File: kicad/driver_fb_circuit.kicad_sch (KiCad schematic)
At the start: 51 parts, among them Q1 IRFZ44N, Q2 IRFZ44N, Q3 IRFZ44N, Q4 IRFZ44N, Q5 IRFZ44N, Q6 IRFZ44N, U1 IR2104, U2 IR2104, U3 IR2104, U4 INA180A2, U7 INA180A2, U8 INA180A2

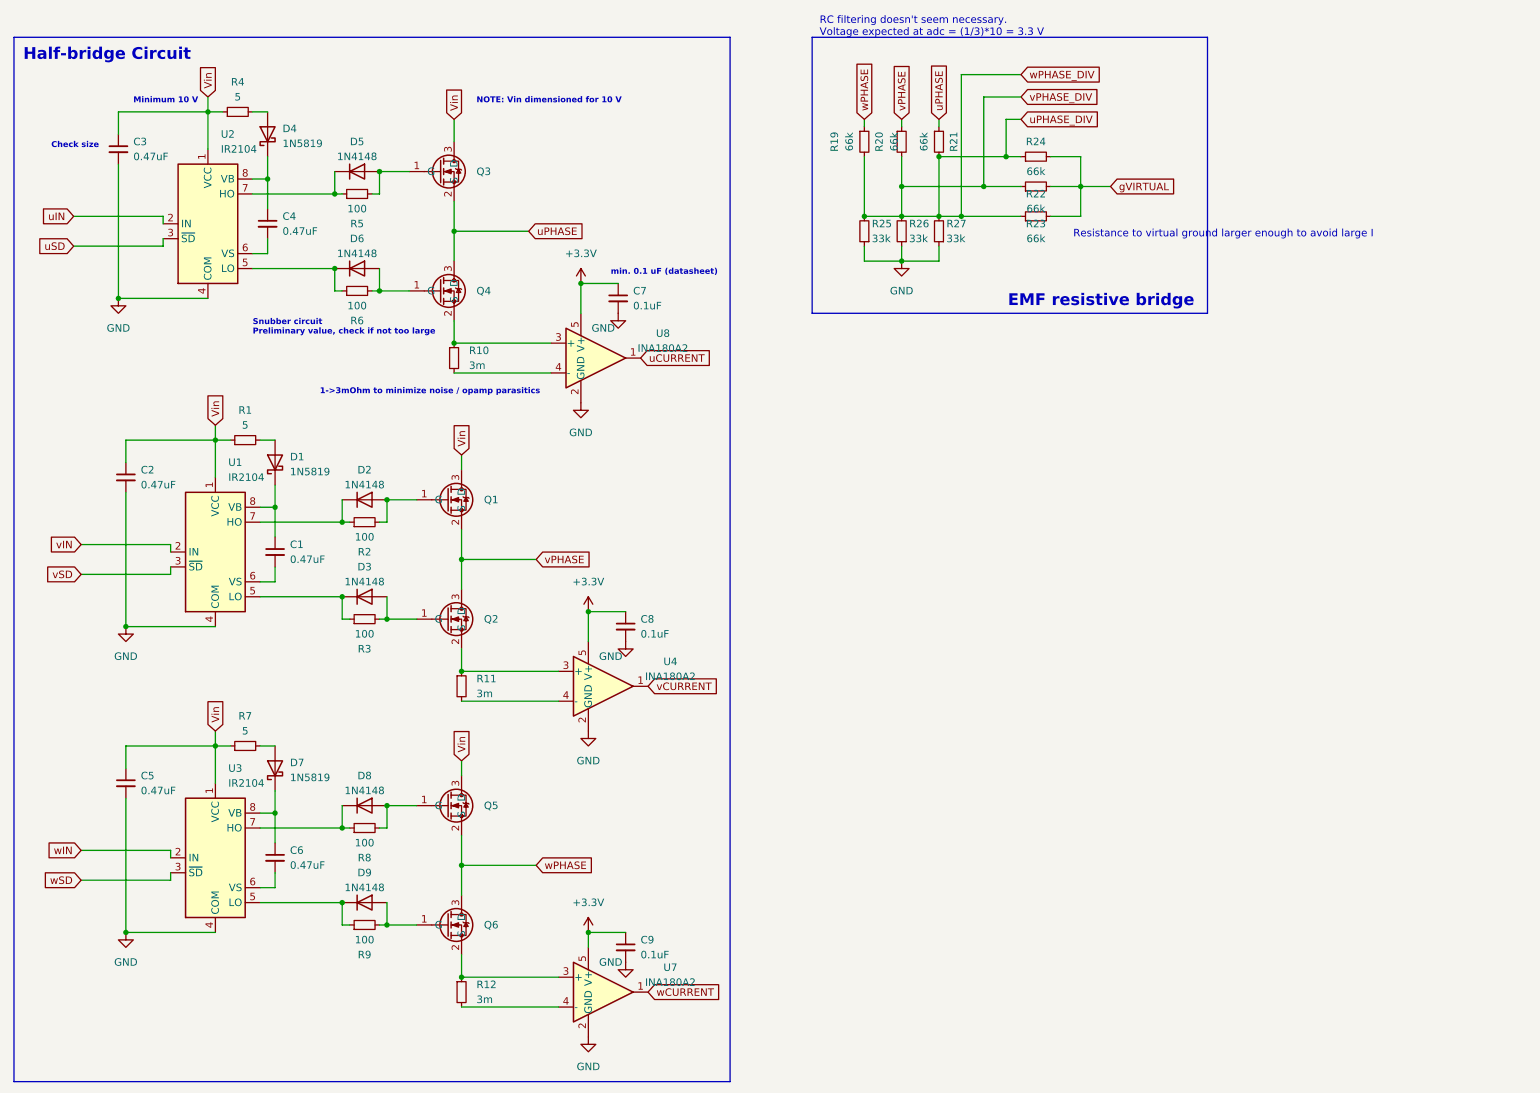
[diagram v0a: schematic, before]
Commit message: [simulations] Added 10 V and 5 V simulations for buck converter, [scripts] Added bulk capacitor requirement notebook [kicad] Fixed buck converter schematic
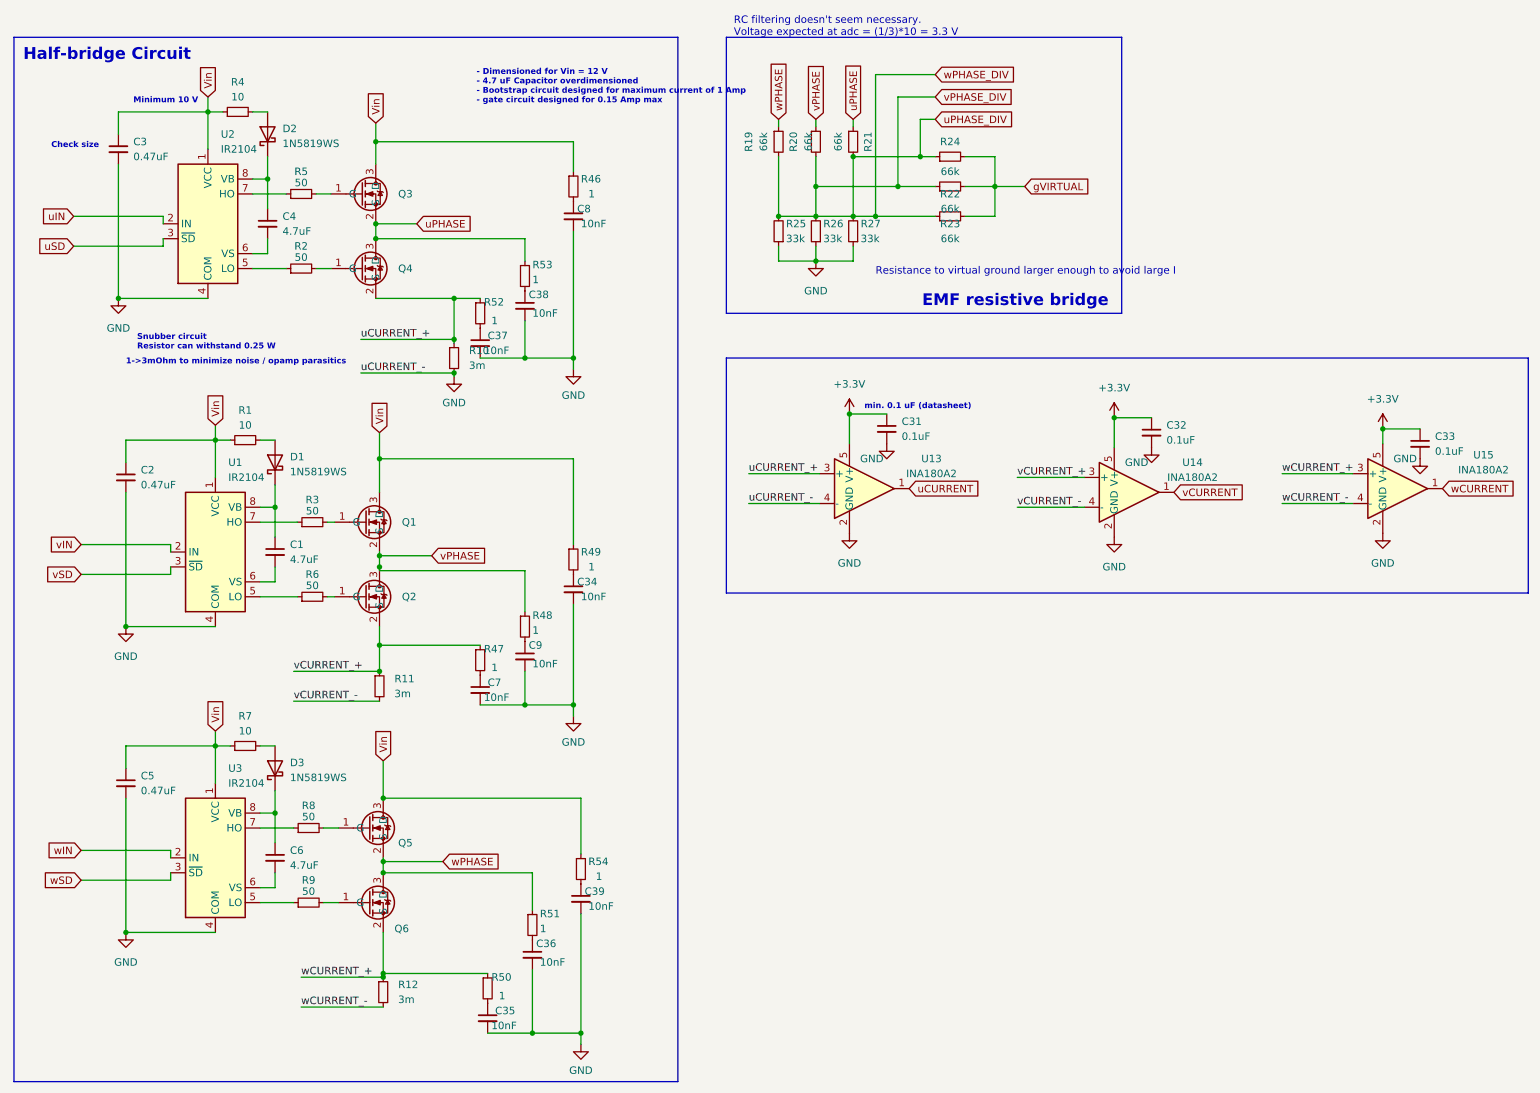
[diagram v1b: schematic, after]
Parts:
- removed D2, D3, D5, D6, D8, D9: 1N4148, Diode_THT:D_DO-35_SOD27_P7.62mm_Horizontal, symbol Diode:1N4148
- removed D4, D7: 1N5819, Diode_THT:D_DO-41_SOD81_P10.16mm_Horizontal, symbol Diode:1N5819
- removed U4, U7, U8: INA180A2, Package_TO_SOT_SMD:SOT-23-5, symbol Amplifier_Current:INA180A2
- added C31, C32, C33: 0.1uF, symbol Device:C_Small
- added C34, C35, C36, C37, C38, C39: 10nF, Capacitor_SMD:C_0402_1005Metric, symbol Device:C_Small
- added D2, D3: 1N5819WS, Diode_SMD:D_SOD-323, symbol Diode:1N5819
- added R46, R47, R48, R49, R50, R51, R52, R53, R54: 1, Resistor_SMD:R_0603_1608Metric, symbol Device:R_Small
- added U13, U14, U15: INA180A2, Package_TO_SOT_SMD:SOT-23-5, symbol Amplifier_Current:INA180A2
- C1, C4, C6: value 0.47uF -> 4.7uF; footprint (none) -> Capacitor_SMD:C_0603_1608Metric; JLCPCB (none) -> C19666
- C7, C8, C9: value 0.1uF -> 10nF; footprint (none) -> Capacitor_SMD:C_0402_1005Metric; JLCPCB (none) -> C15195
- D1: value 1N5819 -> 1N5819WS; footprint Diode_THT:D_DO-41_SOD81_P10.16mm_Horizontal -> Diode_SMD:D_SOD-323; JLCPCB (none) -> C191023
- R1, R4, R7: value 5 -> 10; footprint (none) -> Resistor_SMD:R_1206_3216Metric; JLCPCB (none) -> https://wmsc.lcsc.com/wmsc/upload/file/pdf/v2/lcsc/22060101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
- R2, R3, R5, R6, R8, R9: value 100 -> 50; footprint (none) -> Resistor_SMD:R_1206_3216Metric; JLCPCB (none) -> C5266158
- U1, U2, U3: footprint (none) -> Package_SO:SOIC-8-1EP_3.9x4.9mm_P1.27mm_EP2.29x3mm; JLCPCB (none) -> C5804631
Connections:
- net +3.3V: now also C31.1, C32.1, C33.1, U13.5 (V+), U14.5 (V+), U15.5 (V+); no longer C7.1, C8.1, C9.1
- net GND: now also R10.2, C31.2, C32.2, C33.2, C34.2, C35.2, C36.2, C37.2, C38.2, C39.2, U13.2 (GND), U13.4 (-), U14.2 (GND), U15.2 (GND)
- net Vin: now also R46.1, R49.1, R54.1
- net uCURRENT: now also U13.1
- net uPHASE: now also R53.1
- net vCURRENT: now also U14.1
- net vPHASE: now also R48.1
- net wCURRENT: now also U15.1
- net wPHASE: now also R51.1
- net at R3.1: now also U1.7 (HO); no longer U1.5 (LO)
- net at R3.2: now also Q1.1 (G); no longer Q2.1 (G)
- net at R2.2: now also Q4.1 (G); no longer Q1.1 (G)
- net at R4.2: now also D2.2 (A)
- net at R2.1: now also U2.5 (LO); no longer U1.7 (HO)
- net at R6.1: now also U1.5 (LO); no longer U2.5 (LO)
- net at C4.1, U2.8 (VB): now also D2.1 (K)
- net at R7.2: now also D3.2 (A)
- net wCURRENT_+: now reaches Q6.2 (S), R12.1
- net wCURRENT_+: now also R50.1, U15.3 (+)
- net wCURRENT_-: now reaches R12.2
- net wCURRENT_-: now also U15.4 (-)
- net at C6.1, U3.8 (VB): now also D3.1 (K)
- net at R6.2: now also Q2.1 (G); no longer Q4.1 (G)
- net vCURRENT_+: now reaches Q2.2 (S), R11.1
- net vCURRENT_+: now also R47.1, U14.3 (+)
- net vCURRENT_-: now reaches R11.2
- net vCURRENT_-: now also U14.4 (-)
- net uCURRENT_+: now reaches Q4.2 (S), R10.1
- net uCURRENT_+: now also R52.1, U13.3 (+)
- new net: C7.1, R47.2
- new net: C39.1, R54.2
- new net: C8.1, R46.2
- new net: C38.1, R53.2
- new net: C9.1, R48.2
- new net: C36.1, R51.2
- new net: C35.1, R50.2
- new net: C37.1, R52.2
- new net: C34.1, R49.2
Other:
- note added: "- Dimensioned for Vin = 12 V - 4.7 uF Capacitor overdimensioned - Bootstrap circuit designed for maximum current of 1 Amp - gate circuit designed for 0.15 Amp max"
- note added: "Snubber circuit Resistor can withstand 0.25 W"
- note removed: "NOTE: Vin dimensioned for 10 V"
- note removed: "Snubber circuit Preliminary value, check if not too large"
- moved on the sheet: Q1, Q2, Q3, Q4, Q5, Q6, R11, R12, R19, R20, R21, R22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

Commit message: [kicad] added component numbers from jlcpcb [scripts] added bulk capacitor plot
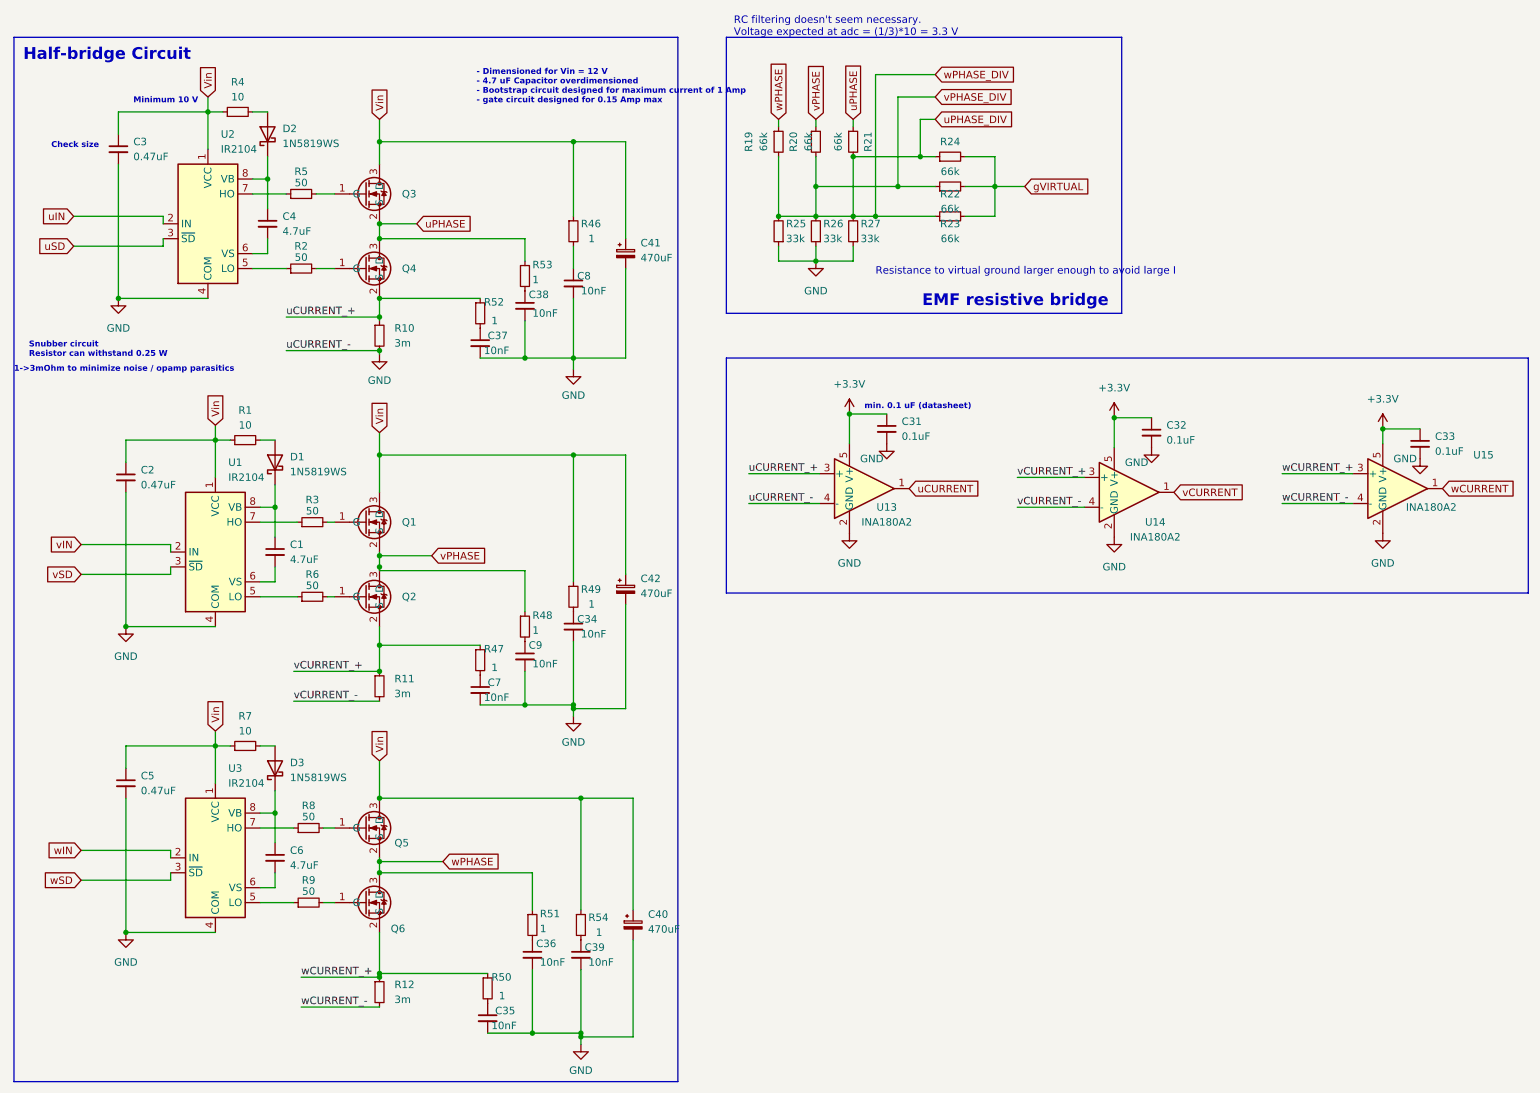
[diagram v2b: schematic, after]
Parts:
- added C40, C41, C42: 470uF, Capacitor_THT:C_Radial_D10.0mm_H20.0mm_P5.00mm, symbol Device:C_Polarized_Small
- C31, C32, C33: footprint (none) -> Resistor_SMD:R_0402_1005Metric; jlcpcb (none) -> C307331
- Q1, Q2, Q3, Q4, Q5, Q6: jlcpcb (none) -> C7429904
- R1, R4, R7: JLCPCB https://wmsc.lcsc.com/wmsc/upload/file/pdf/v2/lcsc/22060101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 -> C17903
- R10, R11, R12: footprint (none) -> Resistor_SMD:R_2512_6332Metric; MFR. (none) -> LR2512D-2W-3mR-1%; jlcpcb (none) -> C500615
- U13, U14, U15: JLCPCB (none) -> C192764
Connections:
- net GND: now also C40.2, C41.2, C42.2
- net Vin: now also C40.1, C41.1, C42.1
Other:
- moved on the sheet: C34, C39, C8, Q3, Q4, Q5, Q6, R46, R49, R54

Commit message: [kicad] Added resistor footprints and mfr numbers, added switching circuit for USB_DP, [simulations] Made switching circuit simulation
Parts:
- added R22, R23, R24: 33k, Resistor_SMD:R_0603_1608Metric, symbol Device:R_Small
- R19, R20, R21: value 66k -> 33k; footprint (none) -> Resistor_SMD:R_0603_1608Metric; jlcpcb (none) -> C4216
- R25, R26, R27: footprint (none) -> Resistor_SMD:R_0603_1608Metric; jlcpcb (none) -> C4216
- R28: renamed from R24; value 66k -> 33k; footprint (none) -> Resistor_SMD:R_0603_1608Metric; jlcpcb (none) -> C4216
- R29: renamed from R22; value 66k -> 33k; footprint (none) -> Resistor_SMD:R_0603_1608Metric; jlcpcb (none) -> C4216
- R30: renamed from R23; value 66k -> 33k; footprint (none) -> Resistor_SMD:R_0603_1608Metric; jlcpcb (none) -> C4216
- renumbered R4 to R1, R52 to R10, R53 to R11, R46 to R12, R47 to R13, R48 to R14, R49 to R15, R50 to R16, R51 to R17, R54 to R18, R1 to R2, R7 to R3, R5 to R4, R2 to R5, R3 to R6, R6 to R7
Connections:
- net Vin: no longer C2.1, C3.1, C5.1, R1.1, R2.1, R3.1, U1.1 (VCC), U2.1 (VCC), U3.1 (VCC)
- net uPHASE: now also R23.2; no longer R21.1
- net uPHASE_DIV: now also R20.1, R22.1, R24.1; no longer R19.2, R20.2, R21.2
- net vPHASE: now also R21.2; no longer R20.1
- net wPHASE: now also R19.2; no longer R19.1
- new net: R23.1, R24.2
- new net: R19.1, R20.2
- new net: R21.1, R22.2
- new net +10V: C2.1, C3.1, C5.1, R1.1, R2.1, R3.1, U1.1 (VCC), U2.1 (VCC), U3.1 (VCC)
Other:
- moved on the sheet: C39, R18, R25, R26, R27, R28, R29, R30

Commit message: [kicad] completed resistor and capacitor BOM, added footprints, streamlined the resistance and capacitance values | TODO: find new crystal, add footprint for CAN driver + button, check IC-footprints [simulations] adapted the simulations according to changes in the schematic [scripts] Added warning for HP 0.33 ohm resistor
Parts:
- removed R2, R3: 10, Resistor_SMD:R_1206_3216Metric, symbol Device:R_Small
- removed R5, R6, R7, R8, R9: 50, Resistor_SMD:R_1206_3216Metric, symbol Device:R_Small
- added R16, R21, R22, R28, R30: 51, Resistor_SMD:R_1206_3216Metric, symbol Device:R_Small
- added R20, R27: 10, Resistor_SMD:R_1206_3216Metric, symbol Device:R_Small
- C1: renamed from C3; footprint (none) -> Capacitor_SMD:C_0805_2012Metric; MFR.Part (none) -> CL21A475KAQNNNE; jlcpcb (none) -> C1779
- C10: renamed from C2; footprint (none) -> Capacitor_SMD:C_0805_2012Metric; MFR.Part (none) -> CL21A475KAQNNNE; jlcpcb (none) -> C1779
- C11: renamed from C1; JLCPCB C19666 -> (none); jlcpcb (none) -> C19666
- C13: renamed from C34; JLCPCB C15195 -> (none); jlcpcb (none) -> C15195
- C14: renamed from C9; JLCPCB C15195 -> (none); jlcpcb (none) -> C15195
- C15: renamed from C7; JLCPCB C15195 -> (none); jlcpcb (none) -> C15195
- C16: renamed from C5; footprint (none) -> Capacitor_SMD:C_0805_2012Metric; MFR.Part (none) -> CL21A475KAQNNNE; jlcpcb (none) -> C1779
- C17: renamed from C6; JLCPCB C19666 -> (none); jlcpcb (none) -> C19666
- C18: renamed from C39; JLCPCB C15195 -> (none); jlcpcb (none) -> C15195
- C2: renamed from C4; JLCPCB C19666 -> (none); jlcpcb (none) -> C19666
- C20: renamed from C36; JLCPCB C15195 -> (none); jlcpcb (none) -> C15195
- C21: renamed from C35; JLCPCB C15195 -> (none); jlcpcb (none) -> C15195
- C4: renamed from C8; JLCPCB C15195 -> (none); jlcpcb (none) -> C15195
- C5: renamed from C38; JLCPCB C15195 -> (none); jlcpcb (none) -> C15195
- C6: renamed from C37; JLCPCB C15195 -> (none); jlcpcb (none) -> C15195
- D1: renamed from D2; JLCPCB C191023 -> (none); MFR.Part (none) -> 1N5819WS; jlcpcb (none) -> C191023
- D2: renamed from D1; JLCPCB C191023 -> (none); MFR.Part (none) -> 1N5819WS; jlcpcb (none) -> C191023
- D3: JLCPCB C191023 -> (none); MFR.Part (none) -> 1N5819WS; jlcpcb (none) -> C191023
- R1: JLCPCB C17903 -> (none); MFR.Part (none) -> 1206W4F100JT5E; jlcpcb (none) -> C17903
- R10: renamed from R4; value 50 -> 51; JLCPCB C5266158 -> (none); MFR.Part (none) -> 1206W4F510JT5E; jlcpcb (none) -> C18019
- R12: JLCPCB C22936 -> (none); jlcpcb (none) -> C22936
- R17: renamed from R11; JLCPCB C22936 -> (none); jlcpcb (none) -> C22936
- R18: renamed from R10; JLCPCB C22936 -> (none)
- R19: renamed from R10; MFR. LR2512D-2W-3mR-1% -> (none); MFR.Part (none) -> LR2512D-2W-3mR-1%
- R23: renamed from R15; JLCPCB C22936 -> (none); jlcpcb (none) -> C22936
- R24: renamed from R14; JLCPCB C22936 -> (none); jlcpcb (none) -> C22936
- R25: renamed from R13; JLCPCB C22936 -> (none); jlcpcb (none) -> C22936
- R26: renamed from R11; MFR. LR2512D-2W-3mR-1% -> (none); MFR.Part (none) -> LR2512D-2W-3mR-1%
- R29: renamed from R18; JLCPCB C22936 -> (none); jlcpcb (none) -> C22936
- R31: renamed from R17; JLCPCB C22936 -> (none); jlcpcb (none) -> C22936
- R32: renamed from R16; JLCPCB C22936 -> (none); jlcpcb (none) -> C22936
- R33: renamed from R12; MFR. LR2512D-2W-3mR-1% -> (none); MFR.Part (none) -> LR2512D-2W-3mR-1%
- U1: renamed from U2; JLCPCB C5804631 -> (none); jlcpcb (none) -> C5804631
- U2: renamed from U13; JLCPCB C192764 -> (none); jlcpcb (none) -> C192764
- U3: renamed from U15; JLCPCB C192764 -> (none); jlcpcb (none) -> C192764
- U4: renamed from U14; JLCPCB C192764 -> (none); jlcpcb (none) -> C192764
- U5: renamed from U1; JLCPCB C5804631 -> (none); jlcpcb (none) -> C5804631
- U6: renamed from U3; JLCPCB C5804631 -> (none); jlcpcb (none) -> C5804631
- renumbered C42 to C12, C40 to C19, C41 to C3, C31 to C7, C32 to C8, C33 to C9, Q3 to Q1, Q4 to Q2, Q1 to Q3, Q2 to Q4, R30 to R11, R25 to R13, R26 to R14, R27 to R15, R23 to R2, R19 to R3, R21 to R4, R24 to R5, R28 to R6, R22 to R7, R20 to R8, R29 to R9
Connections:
- net +10V: now also R20.1, R27.1
- net at Q3.1 (G): now also R21.2
- net at Q5.1 (G): now also R28.2
- net at U1.5 (LO): now also R16.1
- net at D3.2 (A): now also R27.2
- net at U5.7 (HO): now also R21.1
- net at D2.2 (A): now also R20.2
- net at U6.5 (LO): now also R30.1
- net at U6.7 (HO): now also R28.1
- net at Q6.1 (G): now also R30.2
- net at Q4.1 (G): now also R22.2
- net at U5.5 (LO): now also R22.1
- net at Q2.1 (G): now also R16.2
